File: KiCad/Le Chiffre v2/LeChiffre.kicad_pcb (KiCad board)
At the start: 2 copper layers, 228.4 x 85 mm, 105 parts, among them J1 Conn_01x03_Female, J2 Conn_01x04_Female, SW1 SW_Push, SW10 SW_Push, SW11 SW_Push, SW12 SW_Push, SW13 SW_Push, SW14 SW_Push, SW15 SW_Push, SW16 SW_Push, SW17 SW_Push, SW18 SW_Push, SW19 SW_Push, SW2 SW_Push, SW20 SW_Push, SW21 SW_Push, SW22 SW_Push, SW23 SW_Push, SW24 SW_Push, SW25 SW_Push, SW26 SW_Push, SW27 SW_Push, SW28 SW_Push, SW29 SW_Push, SW3 SW_Push, SW30 SW_Push, SW31 SW_Push, SW32 SW_Push, SW33 SW_Push, SW34 SW_Push, SW35 SW_Push, SW36 Rotary_Encoder_Switch, SW37 SW_Push, SW4 SW_Push, SW5 SW_Push, SW6 SW_Push, SW7 SW_Push, SW8 SW_Push, SW9 SW_Push, U1 ATmega32U4-AU, Y1 Crystal_GND2

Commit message: swapped to mcu daughterboard for no good reason
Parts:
- removed C1, C2, C5: .1u, Keebio-Parts:C_0603
- removed C3, C6: 22p, Keebio-Parts:C_0603
- removed C4: 1u, Keebio-Parts:C_0603
- removed F1: Polyfuse_Small, Keebio-Parts:Fuse_0805
- removed R1, R2: 5.1k, Keebio-Parts:R_0805
- removed R3, R4: 22, Keebio-Parts:R_0805
- removed R6: 10k, Keebio-Parts:R_0805
- removed U1: ATmega32U4-AU, Keebio-Parts:ATMEGA32U4-AU
- removed USB1: HRO-TYPE-C-31-M-12, Type-C:HRO-TYPE-C-31-M-12-HandSoldering
- removed Y1: Crystal_GND2, Keebio-Parts:Crystal_SMD_3225-4pin_3.2x2.5mm
- added 74HC595: , 74HC595_SOIC-16_3.9x9.9mm_P1.27mm, F.Cu at (134.1, 106.3)
- added 74HC595: , 74HC595_SOIC-16_3.9x9.9mm_P1.27mm, F.Cu at (143.7, 106.3)
- added ?: combo-controller, 0-jasonhazel-footprints:combo-controller, B.Cu at (136.8, 39.9)
- added kibuzzard-6397B74C: G***, kibuzzard-6397B74C, F.Cu at (136.8, 39.9)
- moved C8 10.9 mm to (128.4, 87.5)
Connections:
- net Net-(R5-Pad2) renamed RST
- net SCK renamed I2C_SCL
- net SDA renamed I2C_SDA
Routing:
- net SPI_SCLK: track 0.00 -> 108.9 mm, vias 0 -> 2
- net SR_CS: track 0.00 -> 104.2 mm, vias 0 -> 1
- net SPI_MOSI: track 0.00 -> 94.8 mm, vias 0 -> 1
- net row2: track 252.5 -> 337.2 mm, vias 2 -> 3
- net /D+: track 78.5 -> 0.00 mm, vias 2 -> 0
- net /D-: track 78.2 -> 0.00 mm, vias 2 -> 0
- net LED: track 13.9 -> 89.6 mm, vias 2 -> 4
- net GND: track 81.7 -> 30.4 mm, vias 38 -> 45
- net row1: track 234.4 -> 276.4 mm, vias 0 -> 2
- net VCC: track 698.2 -> 660.0 mm, vias 13 -> 12
- net RST: track 42.6 -> 68.0 mm
- net row3: track 218.9 -> 242.2 mm, vias 3 -> 2
- net CC1: track 19.5 -> 0.00 mm
- net EncA: track 48.4 -> 30.4 mm, vias 1 -> 0
- net DN-: track 15.7 -> 0.00 mm
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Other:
- board size 228.4 x 85 mm -> 228.4 x 93.3 mm
- net class Default removed
- net class power removed
- board text added: "Bastardized by Jason Hazel 2022"
- board text removed: "Le Chiffre by tominabox1 2020"

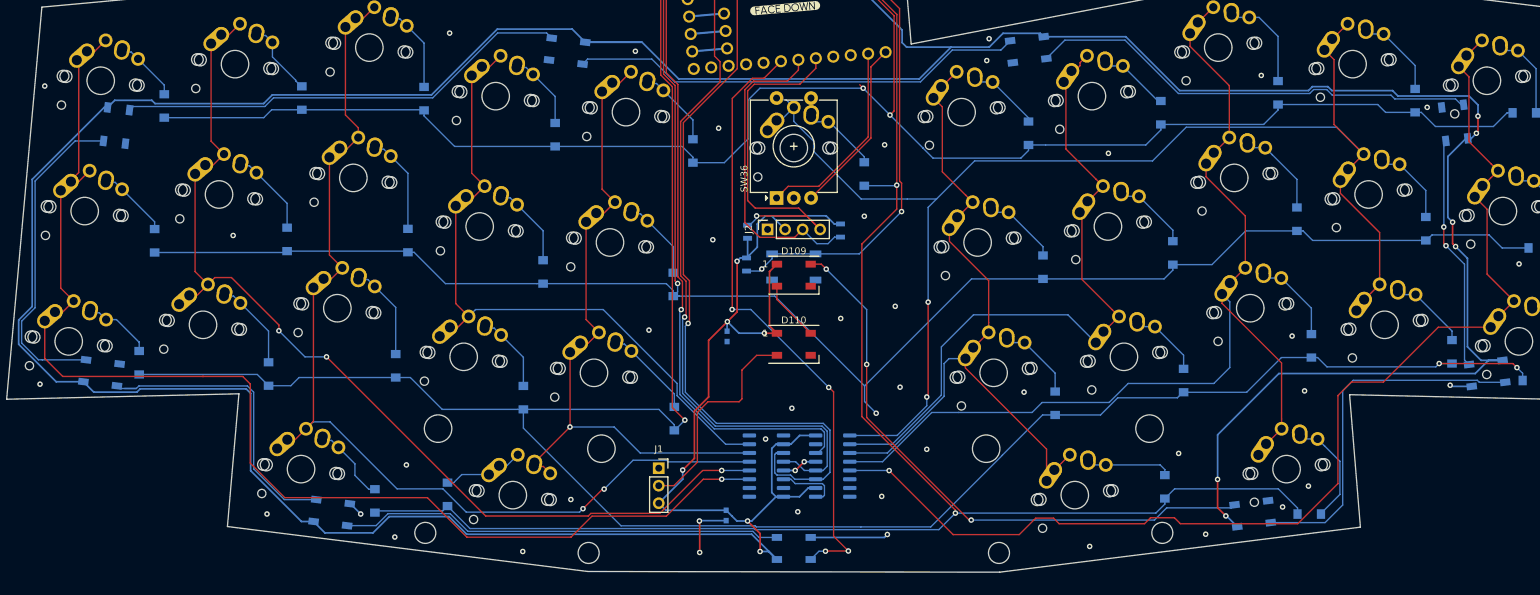
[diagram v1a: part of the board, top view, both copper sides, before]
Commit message: cleanup tracks and vias
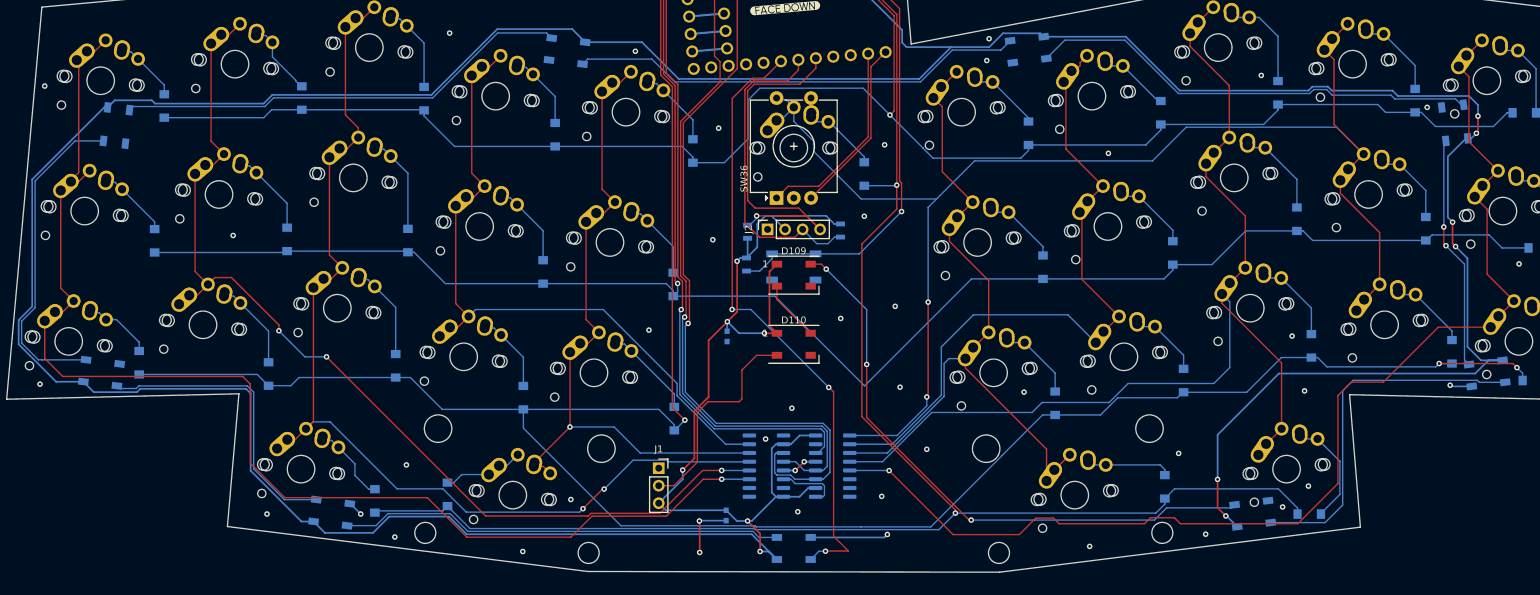
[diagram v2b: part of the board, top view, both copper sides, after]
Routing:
- net VCC: track 660.0 -> 651.6 mm
- net row1: track 276.4 -> 270.8 mm, vias 2 -> 1
- net Net-(D101-Pad2): track 44.3 -> 42.6 mm
- net EncA: track 30.4 -> 29.0 mm
- net col9: track 167.5 -> 166.7 mm
- net col0: track 178.5 -> 177.7 mm
- net row0: track 253.2 -> 252.5 mm, vias 2 -> 1
- net row2: track 337.2 -> 336.6 mm
- net RST: vias 2 -> 1
- net LED: vias 4 -> 3

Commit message: forgot to save
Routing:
- net LED: track 89.6 -> 85.9 mm
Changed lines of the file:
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@@
   (segment (start 243.81 92.88) (end 242.98 92.05) (width 0.2) (layer "B.Cu") (net 7))
   (segment (start 147.790227 115.159989) (end 147.790216 115.16) (width 0.2) (layer "B.Cu") (net 7))
-  (segment (start 143.168664 94.90593) (end 143.149106 94.90593) (width 0.2) (layer "F.Cu") (net 8))
   (segment (start 133.738711 50.070463) (end 136.202026 47.607148) (width 0.2) (layer "F.Cu") (net 8))
+  (segment (start 143.129548 94.925488) (end 143.149106 94.90593) (width 0.2) (layer "F.Cu") (net 8))
   (segment (start 129.134999 52.994161) (end 132.058698 50.070463) (width 0.2) (layer "F.Cu") (net 8))
+  (segment (start 143.839924 95.57719) (end 143.839924 117.510077) (width 0.2) (layer "F.Cu") (net 8))
+  (segment (start 143.149106 94.90593) (end 143.168664 94.90593) (width 0.2) (layer "F.Cu") (net 8))
   (segment (start 143.168664 94.90593) (end 143.839924 95.57719) (width 0.2) (layer "F.Cu") (net 8))
-  (segment (start 143.839924 95.57719) (end 143.839924 116.514827) (width 0.2) (layer "F.Cu") (net 8))
   (segment (start 132.058698 50.070463) (end 133.738711 50.070463) (width 0.2) (layer "F.Cu") (net 8))
-  (segment (start 142.690275 118.659725) (end 142.66 118.69) (width 0.2) (layer "F.Cu") (net 8))
   (segment (start 129.134999 83.591485) (end 129.134999 52.994161) (width 0.2) (layer "F.Cu") (net 8))
-  (segment (start 143.149106 94.90593) (end 143.129548 94.925488) (width 0.2) (layer "F.Cu") (net 8))
-  (segment (start 145.984822 118.659725) (end 142.690275 118.659725) (width 0.2) (layer "F.Cu") (net 8))
   (segment (start 129.110585 83.615899) (end 129.134999 83.591485) (width 0.2) (layer "F.Cu") (net 8))
-  (segment (start 143.839924 116.514827) (end 145.984822 118.659725) (width 0.2) (layer "F.Cu") (net 8))
+  (segment (start 143.839924 117.510077) (end 142.66 118.69) (width 0.2) (layer "F.Cu") (net 8))
   (via (at 143.129548 94.925488) (size 0.8) (drill 0.4) (layers "F.Cu" "B.Cu") (net 8))
   (via (at 129.110585 83.615899) (size 0.8) (drill 0.4) (layers "F.Cu" "B.Cu") (net 8))
